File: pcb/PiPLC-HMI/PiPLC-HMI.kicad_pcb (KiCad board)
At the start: 2 copper layers, 98 x 50 mm, 23 parts, among them J1 Conn_02x12_Odd_Even, J2 KNX

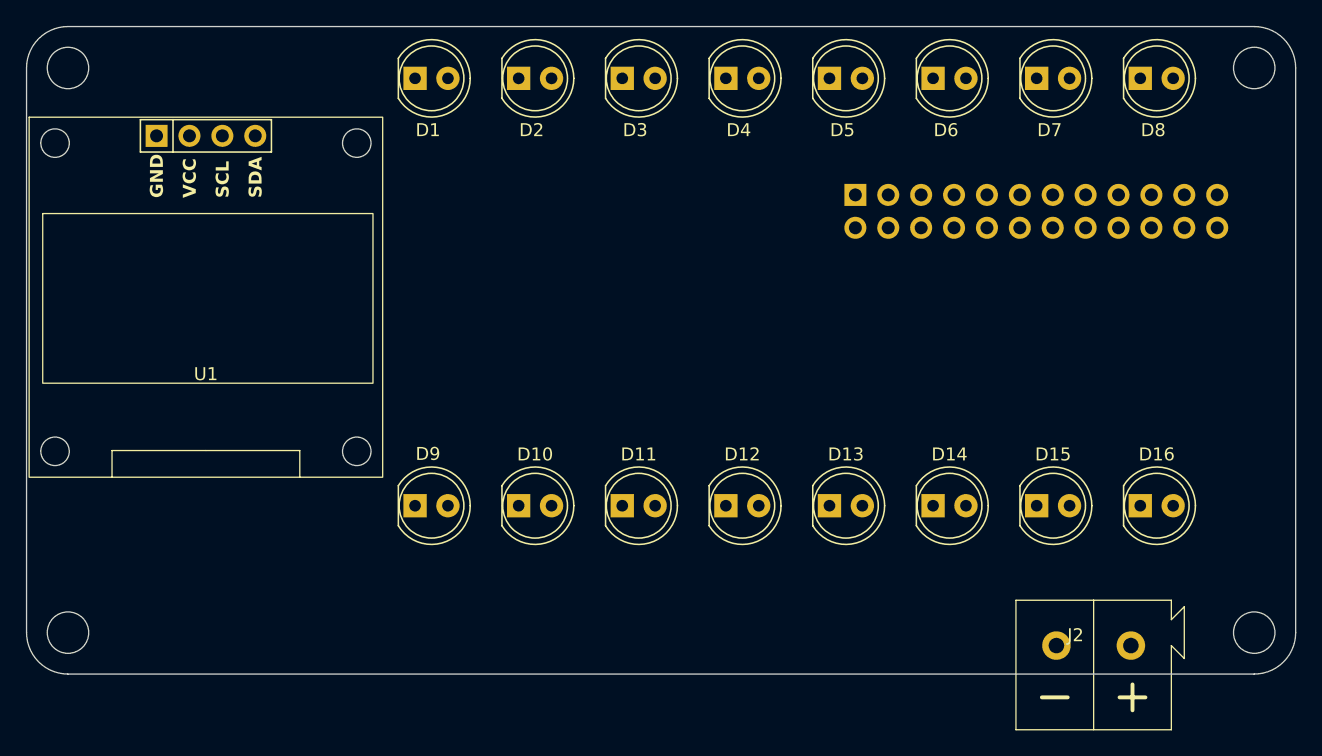
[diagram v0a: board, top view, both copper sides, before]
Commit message: [Mainboard][HMI] Remove display
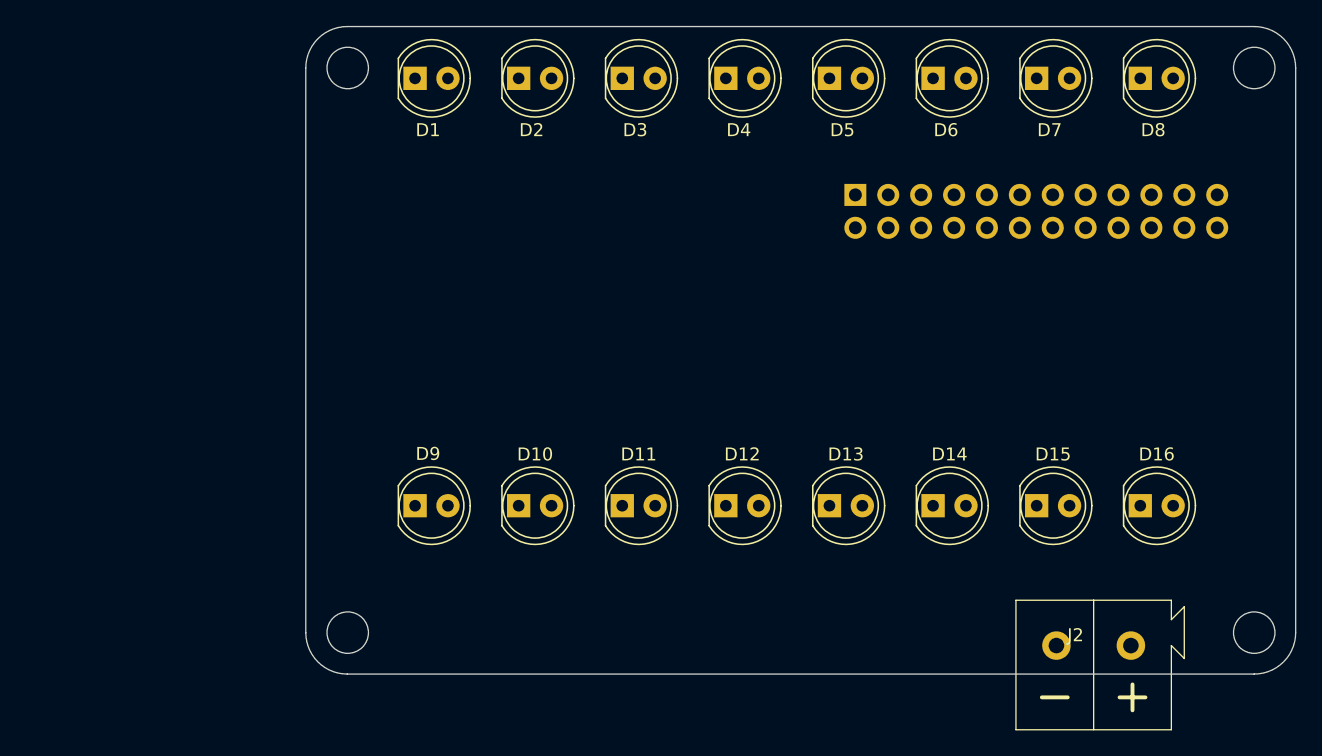
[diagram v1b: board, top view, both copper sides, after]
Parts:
- removed U1: ~, MeineBib:HS96L03
- moved MK2 21.6 mm to (142.7, 70.0)
- moved MK2 21.6 mm to (142.7, 113.6)
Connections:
- J1 pad 1: /I²C SCL -> unconnected-(J1-Pin_1-Pad1)
- J1 pad 3: /I²C SDA -> unconnected-(J1-Pin_3-Pad3)
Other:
- board size 98 x 50 mm -> 76.4 x 50 mm

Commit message: Add "5V OK" and "24V OK" LEDs to HMI
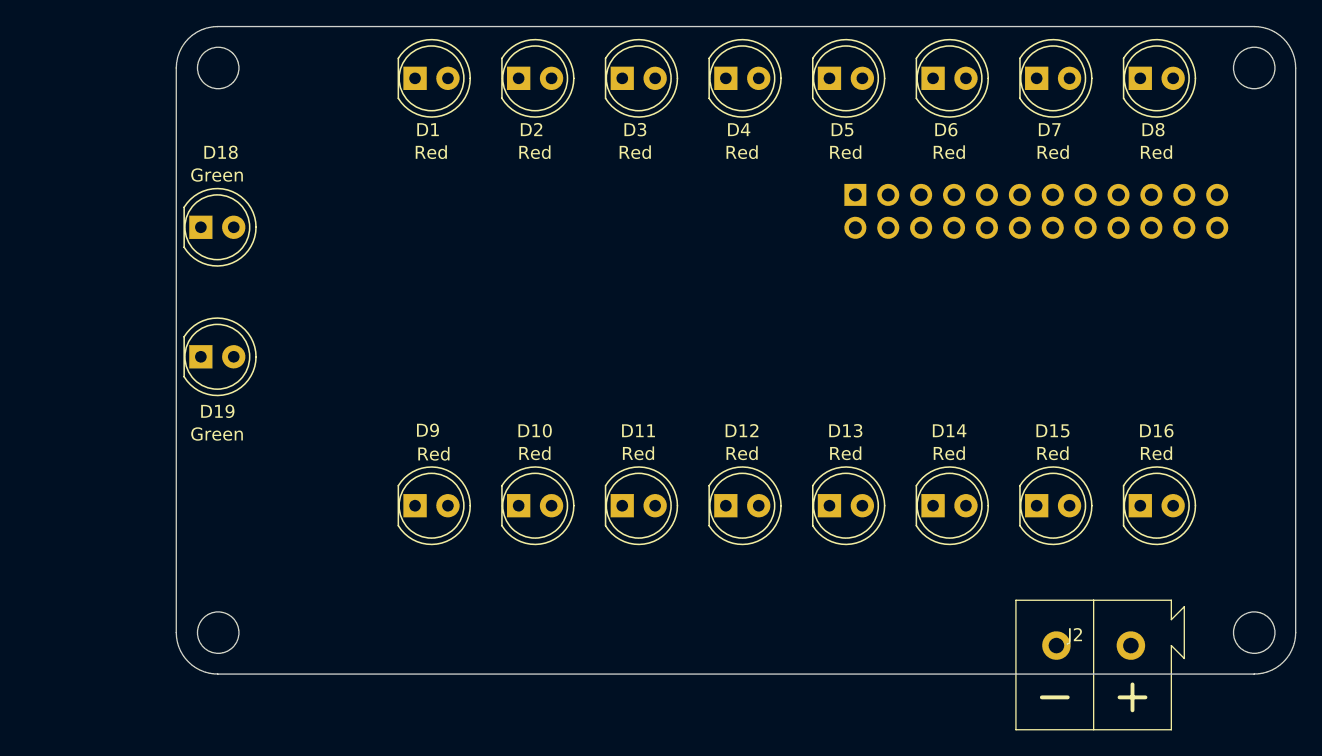
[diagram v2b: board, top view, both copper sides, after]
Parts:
- added D18: Green, LED_THT:LED_D5.0mm, F.Cu at (131.4, 82.3)
- added D19: Green, LED_THT:LED_D5.0mm, F.Cu at (131.4, 92.3)
- D1, D10, D11, D12, D13, D14, D15, D16, D2, D3, D4, D5, D6, D7, D8, D9: value LED -> Red
- moved MK2 10.0 mm to (132.7, 70.0)
- moved MK2 10.0 mm to (132.7, 113.6)
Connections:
- J1 pad 3: unconnected-(J1-Pin_3-Pad3) -> GND
- J1 pad 4: unconnected-(J1-Pin_4-Pad4) -> /LED_24V
- J1 pad 6: GND -> /LED_5V
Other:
- board size 76.4 x 50 mm -> 86.4 x 50 mm

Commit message: [HMI] Flip pin assignment of boardboard interface
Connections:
- J1 pad 10: /LED_I1 -> /LED_Q8
- J1 pad 11: /LED_Q7 -> /LED_I2
- J1 pad 12: /LED_I2 -> /LED_Q7
- J1 pad 13: /LED_Q6 -> /LED_I3
- J1 pad 14: /LED_I3 -> /LED_Q6
- J1 pad 15: /LED_Q5 -> /LED_I4
- J1 pad 16: /LED_I4 -> /LED_Q5
- J1 pad 17: /LED_Q4 -> /LED_I5
- J1 pad 18: /LED_I5 -> /LED_Q4
- J1 pad 19: /LED_Q3 -> /LED_I6
- J1 pad 20: /LED_I6 -> /LED_Q3
- J1 pad 21: /LED_Q2 -> /LED_I7
- J1 pad 22: /LED_I7 -> /LED_Q2
- J1 pad 23: /LED_Q1 -> /LED_I8
- J1 pad 24: /LED_I8 -> /LED_Q1
- J1 pad 3: GND -> /LED_24V
- J1 pad 4: /LED_24V -> GND
- J1 pad 5: /KNX - -> /LED_5V
- J1 pad 6: /LED_5V -> /KNX -
- J1 pad 7: /KNX + -> +3V3
- J1 pad 8: +3V3 -> /KNX +
- J1 pad 9: /LED_Q8 -> /LED_I1
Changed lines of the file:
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@@
       (stroke (width 0.1) (type solid)) (layer "B.Fab"))
     (pad "1" thru_hole rect (at 0 0 270) (size 1.7 1.7) (drill 1) (layers "*.Cu" "*.Mask")
-      (net 19 "unconnected-(J1-Pin_1-Pad1)") (pinfunction "Pin_1") (pintype "passive"))
+      (net 19 "unconnected-(J1-Pin_1-Pad1)") (pinfunction "Pin_1") (pintype "passive+no_connect"))
     (pad "2" thru_hole oval (at 2.54 0 270) (size 1.7 1.7) (drill 1) (layers "*.Cu" "*.Mask")
-      (net 20 "unconnected-(J1-Pin_2-Pad2)") (pinfunction "Pin_2") (pintype "passive"))
+      (net 20 "unconnected-(J1-Pin_2-Pad2)") (pinfunction "Pin_2") (pintype "passive+no_connect"))
     (pad "3" thru_hole oval (at 0 -2.54 270) (size 1.7 1.7) (drill 1) (layers "*.Cu" "*.Mask")
-      (net 10 "GND") (pinfunction "Pin_3") (pintype "passive"))
+      (net 22 "/LED_24V") (pinfunction "Pin_3") (pintype "passive"))
     (pad "4" thru_hole oval (at 2.54 -2.54 270) (size 1.7 1.7) (drill 1) (layers "*.Cu" "*.Mask")
-      (net 22 "/LED_24V") (pinfunction "Pin_4") (pintype "passive"))
+      (net 10 "GND") (pinfunction "Pin_4") (pintype "passive"))
     (pad "5" thru_hole oval (at 0 -5.08 270) (size 1.7 1.7) (drill 1) (layers "*.Cu" "*.Mask")
-      (net 23 "/KNX -") (pinfunction "Pin_5") (pintype "passive"))
+      (net 21 "/LED_5V") (pinfunction "Pin_5") (pintype "passive"))
     (pad "6" thru_hole oval (at 2.54 -5.08 270) (size 1.7 1.7) (drill 1) (layers "*.Cu" "*.Mask")
-      (net 21 "/LED_5V") (pinfunction "Pin_6") (pintype "passive"))
+      (net 23 "/KNX -") (pinfunction "Pin_6") (pintype "passive"))
     (pad "7" thru_hole oval (at 0 -7.62 270) (size 1.7 1.7) (drill 1) (layers "*.Cu" "*.Mask")
-      (net 24 "/KNX +") (pinfunction "Pin_7") (pintype "passive"))
+      (net 2 "+3V3") (pinfunction "Pin_7") (pintype "passive"))
     (pad "8" thru_hole oval (at 2.54 -7.62 270) (size 1.7 1.7) (drill 1) (layers "*.Cu" "*.Mask")
-      (net 2 "+3V3") (pinfunction "Pin_8") (pintype "passive"))
+      (net 24 "/KNX +") (pinfunction "Pin_8") (pintype "passive"))
     (pad "9" thru_hole oval (at 0 -10.16 270) (size 1.7 1.7) (drill 1) (layers "*.Cu" "*.Mask")
-      (net 11 "/LED_Q8") (pinfunction "Pin_9") (pintype "passive"))
+      (net 1 "/LED_I1") (pinfunction "Pin_9") (pintype "passive"))
     (pad "10" thru_hole oval (at 2.54 -10.16 270) (size 1.7 1.7) (drill 1) (layers "*.Cu" "*.Mask")
-      (net 1 "/LED_I1") (pinfunction "Pin_10") (pintype "passive"))
+      (net 11 "/LED_Q8") (pinfunction "Pin_10") (pintype "passive"))
     (pad "11" thru_hole oval (at 0 -12.7 270) (size 1.7 1.7) (drill 1) (layers "*.Cu" "*.Mask")
-      (net 12 "/LED_Q7") (pinfunction "Pin_11") (pintype "passive"))
+      (net 3 "/LED_I2") (pinfunction "Pin_11") (pintype "passive"))
     (pad "12" thru_hole oval (at 2.54 -12.7 270) (size 1.7 1.7) (drill 1) (layers "*.Cu" "*.Mask")
-      (net 3 "/LED_I2") (pinfunction "Pin_12") (pintype "passive"))
+      (net 12 "/LED_Q7") (pinfunction "Pin_12") (pintype "passive"))
     (pad "13" thru_hole oval (at 0 -15.24 270) (size 1.7 1.7) (drill 1) (layers "*.Cu" "*.Mask")
-      (net 13 "/LED_Q6") (pinfunction "Pin_13") (pintype "passive"))
+      (net 4 "/LED_I3") (pinfunction "Pin_13") (pintype "passive"))
     (pad "14" thru_hole oval (at 2.54 -15.24 270) (size 1.7 1.7) (drill 1) (layers "*.Cu" "*.Mask")
-      (net 4 "/LED_I3") (pinfunction "Pin_14") (pintype "passive"))
+      (net 13 "/LED_Q6") (pinfunction "Pin_14") (pintype "passive"))
     (pad "15" thru_hole oval (at 0 -17.78 270) (size 1.7 1.7) (drill 1) (layers "*.Cu" "*.Mask")
-      (net 14 "/LED_Q5") (pinfunction "Pin_15") (pintype "passive"))
+      (net 5 "/LED_I4") (pinfunction "Pin_15") (pintype "passive"))
     (pad "16" thru_hole oval (at 2.54 -17.78 270) (size 1.7 1.7) (drill 1) (layers "*.Cu" "*.Mask")
-      (net 5 "/LED_I4") (pinfunction "Pin_16") (pintype "passive"))
+      (net 14 "/LED_Q5") (pinfunction "Pin_16") (pintype "passive"))
     (pad "17" thru_hole oval (at 0 -20.32 270) (size 1.7 1.7) (drill 1) (layers "*.Cu" "*.Mask")
-      (net 15 "/LED_Q4") (pinfunction "Pin_17") (pintype "passive"))
+      (net 6 "/LED_I5") (pinfunction "Pin_17") (pintype "passive"))
     (pad "18" thru_hole oval (at 2.54 -20.32 270) (size 1.7 1.7) (drill 1) (layers "*.Cu" "*.Mask")
-      (net 6 "/LED_I5") (pinfunction "Pin_18") (pintype "passive"))
+      (net 15 "/LED_Q4") (pinfunction "Pin_18") (pintype "passive"))
     (pad "19" thru_hole oval (at 0 -22.86 270) (size 1.7 1.7) (drill 1) (layers "*.Cu" "*.Mask")
-      (net 16 "/LED_Q3") (pinfunction "Pin_19") (pintype "passive"))
+      (net 7 "/LED_I6") (pinfunction "Pin_19") (pintype "passive"))
     (pad "20" thru_hole oval (at 2.54 -22.86 270) (size 1.7 1.7) (drill 1) (layers "*.Cu" "*.Mask")
-      (net 7 "/LED_I6") (pinfunction "Pin_20") (pintype "passive"))
+      (net 16 "/LED_Q3") (pinfunction "Pin_20") (pintype "passive"))
     (pad "21" thru_hole oval (at 0 -25.4 270) (size 1.7 1.7) (drill 1) (layers "*.Cu" "*.Mask")
-      (net 17 "/LED_Q2") (pinfunction "Pin_21") (pintype "passive"))
+      (net 8 "/LED_I7") (pinfunction "Pin_21") (pintype "passive"))
     (pad "22" thru_hole oval (at 2.54 -25.4 270) (size 1.7 1.7) (drill 1) (layers "*.Cu" "*.Mask")
-      (net 8 "/LED_I7") (pinfunction "Pin_22") (pintype "passive"))
+      (net 17 "/LED_Q2") (pinfunction "Pin_22") (pintype "passive"))
     (pad "23" thru_hole oval (at 0 -27.94 270) (size 1.7 1.7) (drill 1) (layers "*.Cu" "*.Mask")
-      (net 18 "/LED_Q1") (pinfunction "Pin_23") (pintype "passive"))
+      (net 9 "/LED_I8") (pinfunction "Pin_23") (pintype "passive"))
     (pad "24" thru_hole oval (at 2.54 -27.94 270) (size 1.7 1.7) (drill 1) (layers "*.Cu" "*.Mask")
-      (net 9 "/LED_I8") (pinfunction "Pin_24") (pintype "passive"))
+      (net 18 "/LED_Q1") (pinfunction "Pin_24") (pintype "passive"))
     (model "${KICAD6_3DMODEL_DIR}/Connector_PinHeader_2.54mm.3dshapes/PinHeader_2x12_P2.54mm_Vertical.wrl"
       (offset (xyz 0 0 0))

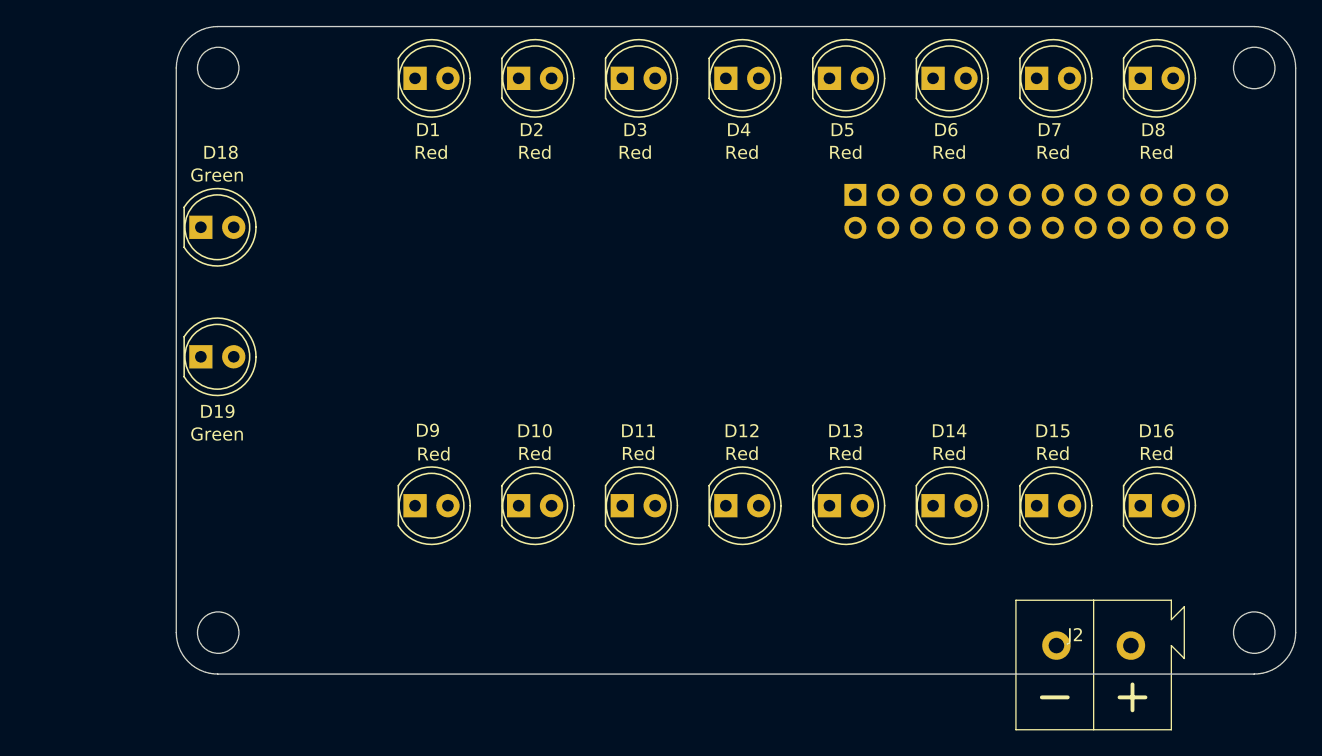
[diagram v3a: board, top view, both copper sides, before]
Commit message: [HMI] Route and beautify
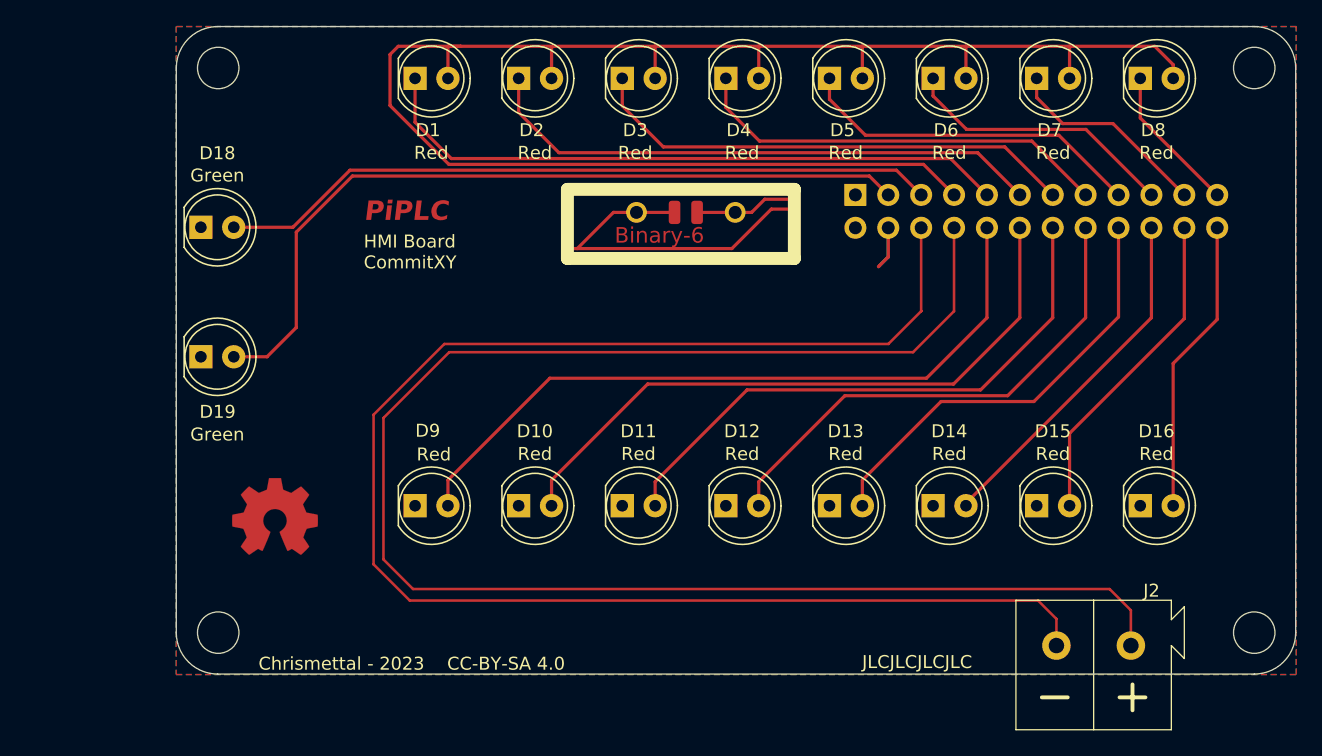
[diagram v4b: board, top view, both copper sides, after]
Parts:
- added H7: Symbol_Binary6, MeineBib:Binary_6_v0.1, F.Cu at (168.8, 82.1)
- added REF**: OSHW-Symbol_6.7x6mm_Copper, Symbol:OSHW-Symbol_6.7x6mm_Copper, F.Cu at (137.1, 104.6)
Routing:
- net +3V3: track 0.00 -> 131.1 mm
- net /KNX +: track 0.00 -> 126.9 mm
- net /KNX -: track 0.00 -> 120.1 mm
- net /LED_24V: track 0.00 -> 61.2 mm
- net /LED_Q8: track 0.00 -> 55.7 mm
- net /LED_5V: track 0.00 -> 55.7 mm
- net /LED_Q7: track 0.00 -> 50.3 mm
- net /LED_I1: track 0.00 -> 49.9 mm
- net /LED_Q6: track 0.00 -> 44.7 mm
- net /LED_I2: track 0.00 -> 44.0 mm
- net /LED_Q5: track 0.00 -> 39.3 mm
- net /LED_I3: track 0.00 -> 38.2 mm
- net /LED_Q4: track 0.00 -> 33.9 mm
- net /LED_I4: track 0.00 -> 32.8 mm
- net /LED_Q3: track 0.00 -> 27.4 mm
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- added copper zone on B.Cu, net GND
- added copper zone on F.Cu, net GND
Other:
- board text added: "Chrismettal - 2023 CC-BY-SA 4.0"
- board text added: "HMI Board CommitXY"
- board text added: "JLCJLCJLCJLC"
- board text added: "PiPLC"

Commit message: Order all PCBs
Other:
- board text added: "HMI Board 8259c5f"
- board text removed: "HMI Board CommitXY"
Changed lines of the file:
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@@
     (effects (font (size 1 1) (thickness 0.15)) (justify left bottom))
   )
-  (gr_text "HMI Board\nCommitXY" (at 143.935 85.596) (layer "F.SilkS")
+  (gr_text "HMI Board\n8259c5f" (at 143.935 85.596) (layer "F.SilkS")
     (effects (font (size 1 1) (thickness 0.15)) (justify left bottom))
   )
